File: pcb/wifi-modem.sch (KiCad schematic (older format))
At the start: 52 parts, among them J1 USB_B, J2 AudioJack3, J3 RS232 DB9, Q1 BC846BDW1, SW1 SW_Push, U1 ESP-12F, U2 74HC245, U3 LM1117-3.3, U4 FT232RL, U5 MAX232

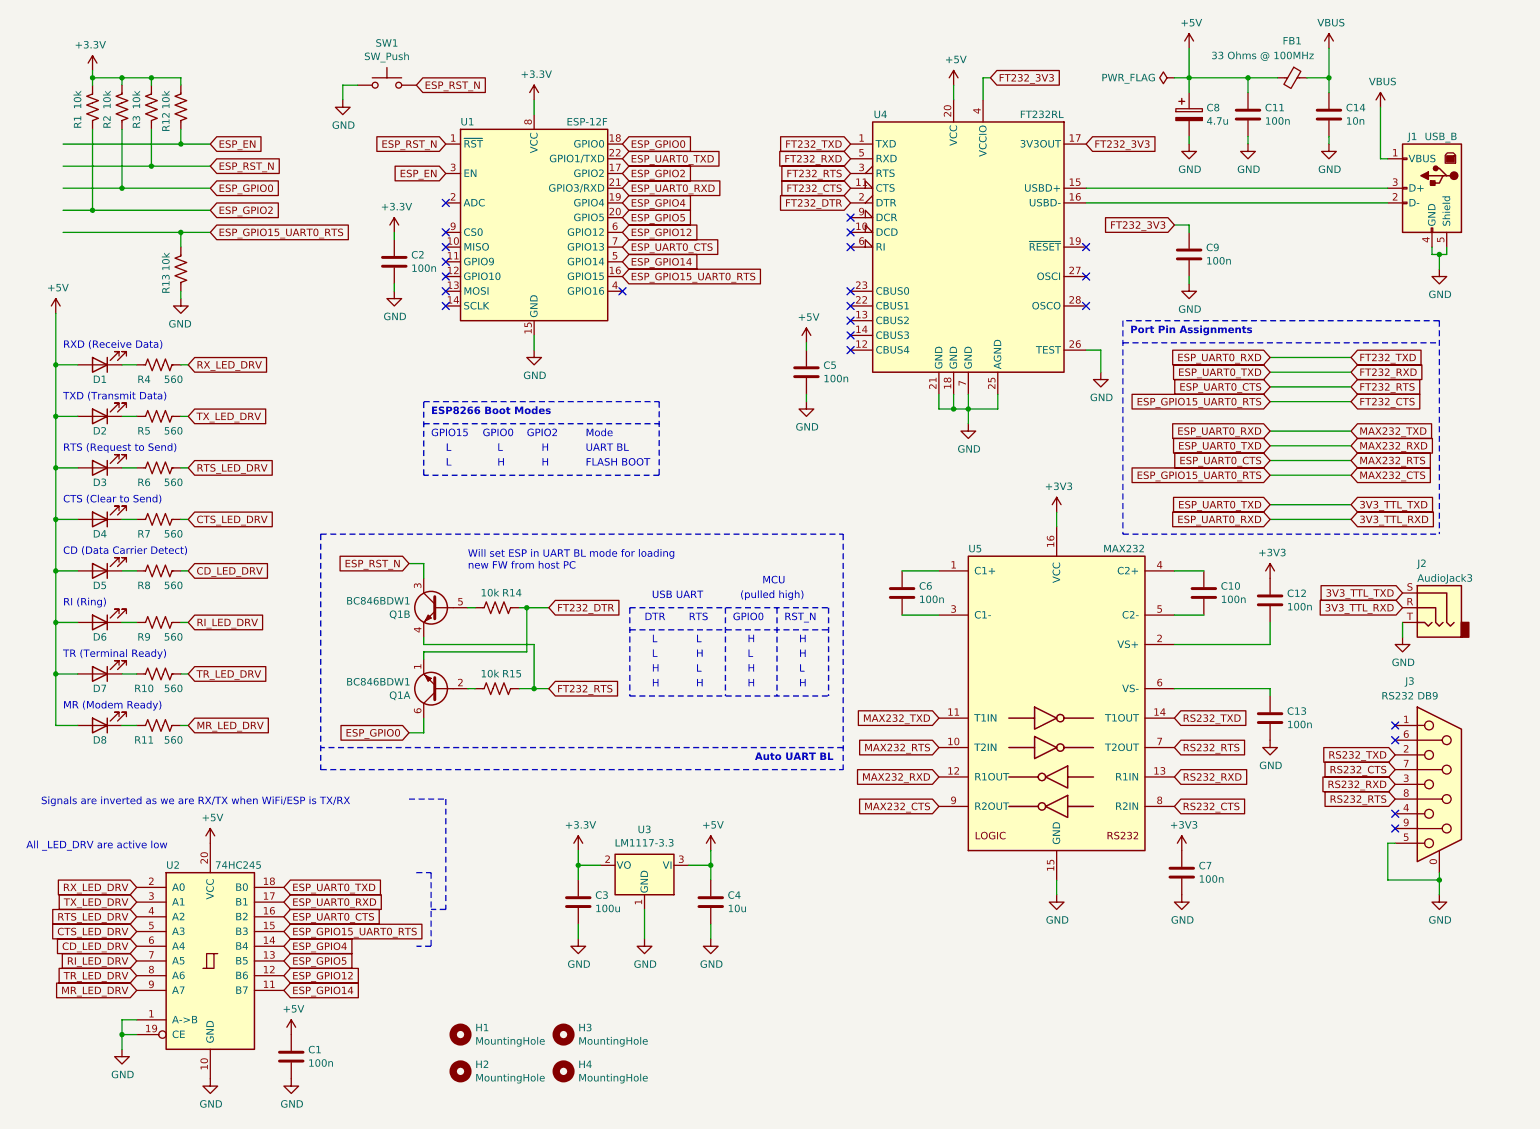
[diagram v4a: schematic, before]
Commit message: Updating date and fixing swapped MAX232 pins
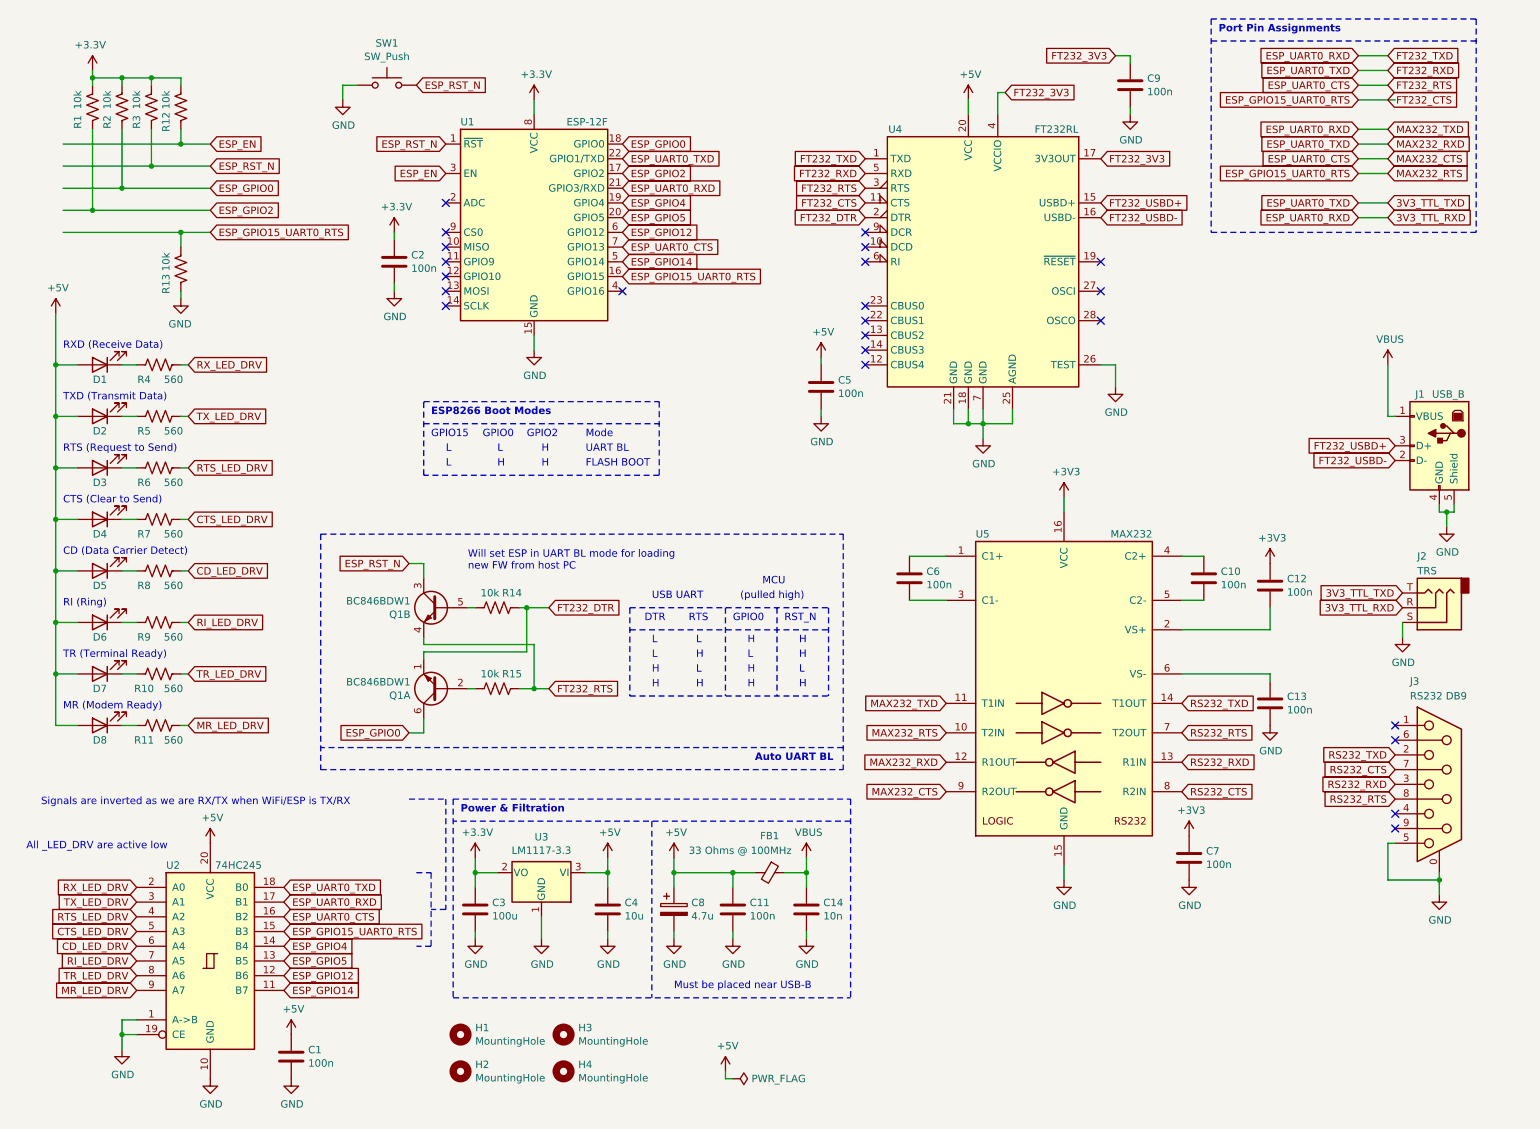
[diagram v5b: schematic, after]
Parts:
- J2: value AudioJack3 -> TRS
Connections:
- net labels added: FT232_USBD+, FT232_USBD-
- wire segments 156 -> 155
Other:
- note added: "Must be placed near USB-B"
- note added: "Power & Filtration"
- moved on the sheet: C10, C11, C12, C13, C14, C3, C4, C5, C6, C7, C8, C9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

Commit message: Beautification
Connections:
- wire segments 155 -> 154
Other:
- note added: "All signals are active low"
- note added: "ESP8266"
- note added: "LEDs & Driver"
- note added: "Ports"
- note added: "RS232 -> UART"
- note added: "USB -> UART"
- note removed: "All _LED_DRV are active low"
- moved on the sheet: C10, C12, C13, C2, C6, C7, D1, D2, D3, D4, D5, D6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

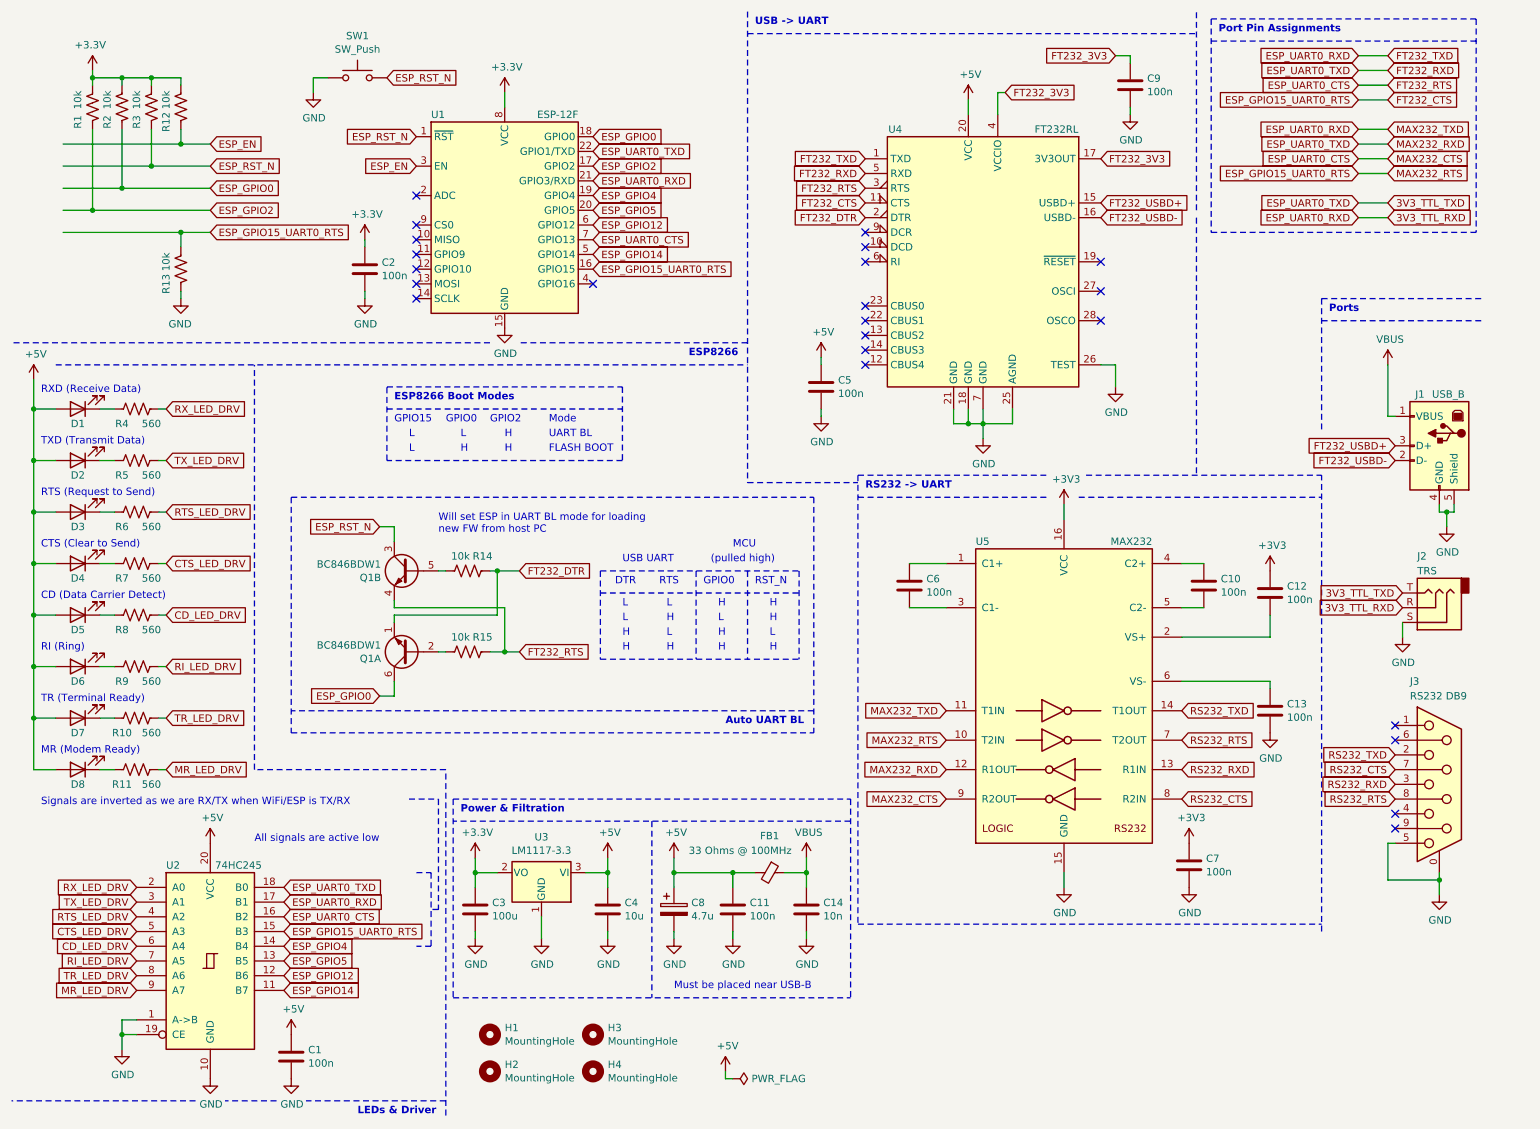
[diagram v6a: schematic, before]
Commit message: Added 100nF cap between RST_N and GND and additional 10uF cap near 3.3V rail of ESP module
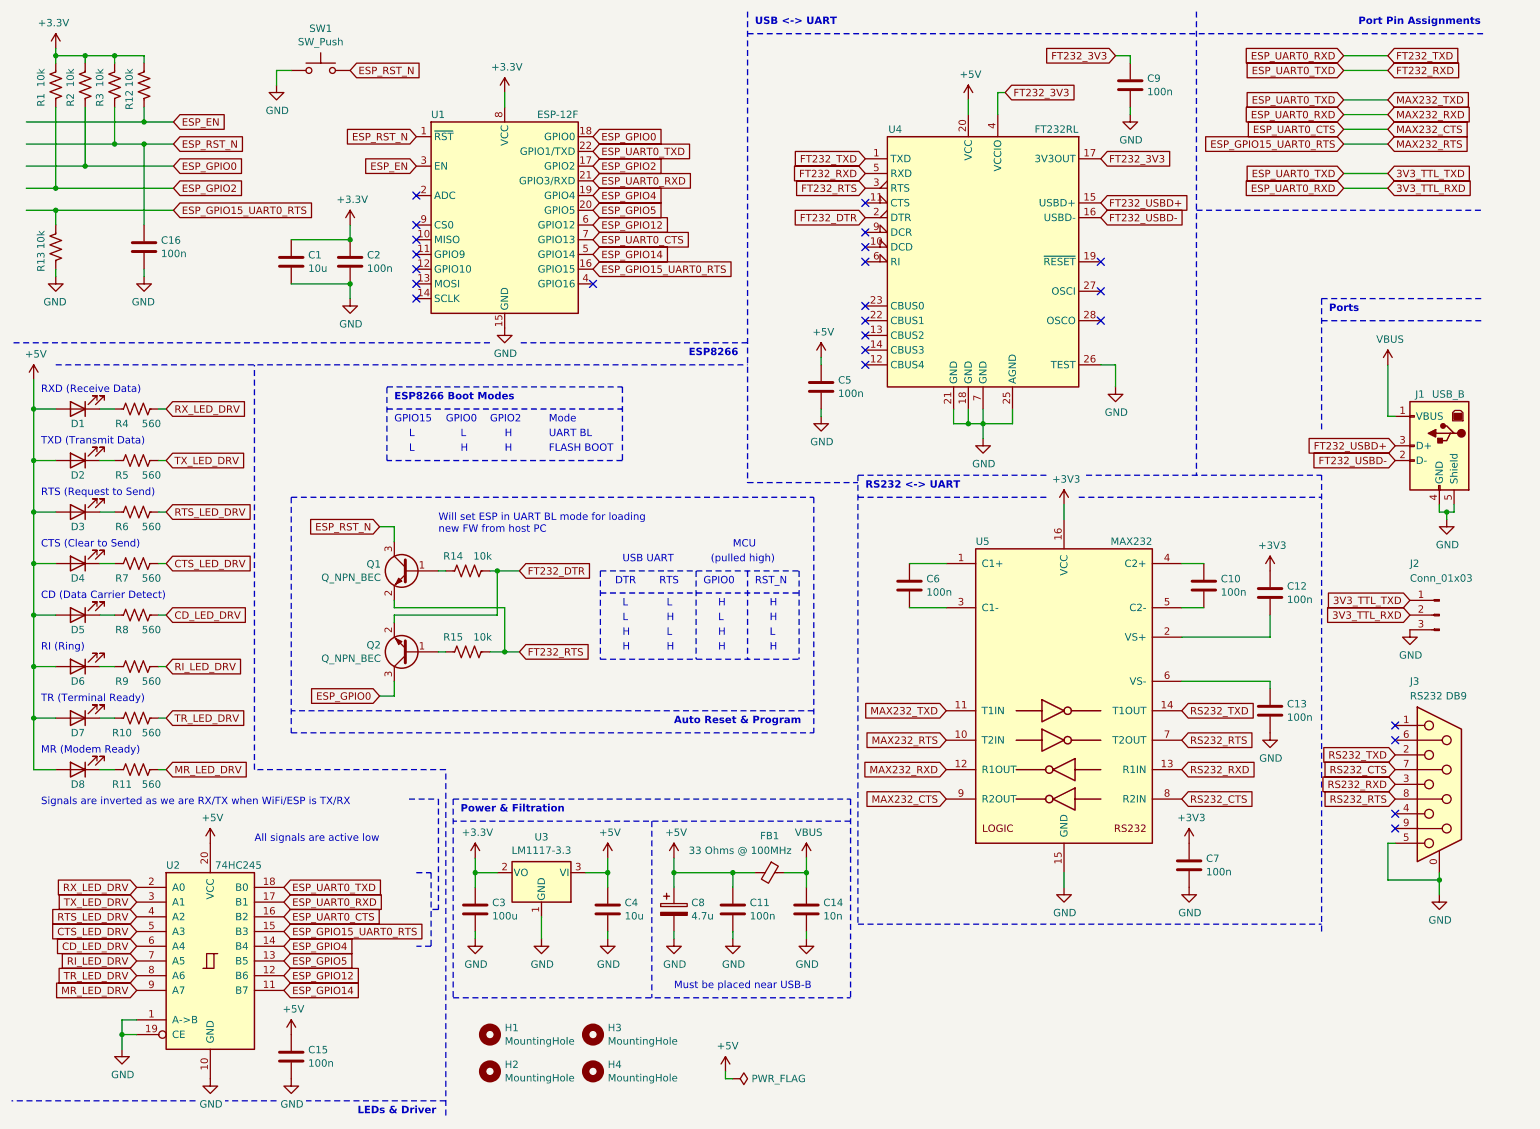
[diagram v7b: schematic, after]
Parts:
- removed J2: TRS, Connector_Audio:Jack_3.5mm_CUI_SJ1-3533NG_Horizontal_CircularHoles, symbol Connector:AudioJack3
- removed Q1: BC846BDW1, Package_TO_SOT_SMD:SOT-363_SC-70-6, symbol Transistor_BJT:BC846BDW1
- added C1: 10u, Capacitor_SMD:C_0805_2012Metric_Pad1.15x1.40mm_HandSolder, symbol Device:C
- added C16: 100n, Capacitor_SMD:C_0805_2012Metric_Pad1.15x1.40mm_HandSolder, symbol Device:C
- added J2: Conn_01x03, Connector_PinHeader_2.54mm:PinHeader_1x03_P2.54mm_Vertical, symbol Connector:Conn_01x03_Male
- added Q1, Q2: Q_NPN_BEC, Package_TO_SOT_SMD:SOT-23, symbol Device:Q_NPN_BEC
- renumbered C1 to C15
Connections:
- net labels removed: FT232_CTS
- wire segments 154 -> 156
- no-connect marks 23 -> 24
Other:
- note added: "Auto Reset & Program"
- note added: "RS232 <-> UART"
- note added: "USB <-> UART"
- note removed: "Auto UART BL"
- note removed: "RS232 -> UART"
- note removed: "USB -> UART"
- moved on the sheet: C2, R1, R12, R13, R2, R3, SW1
